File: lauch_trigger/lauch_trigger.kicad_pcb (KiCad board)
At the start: 2 copper layers, 39 x 22 mm, 6 parts, among them J1 jack_A, J2 jack_B, J3 conn_A, J4 conn_B

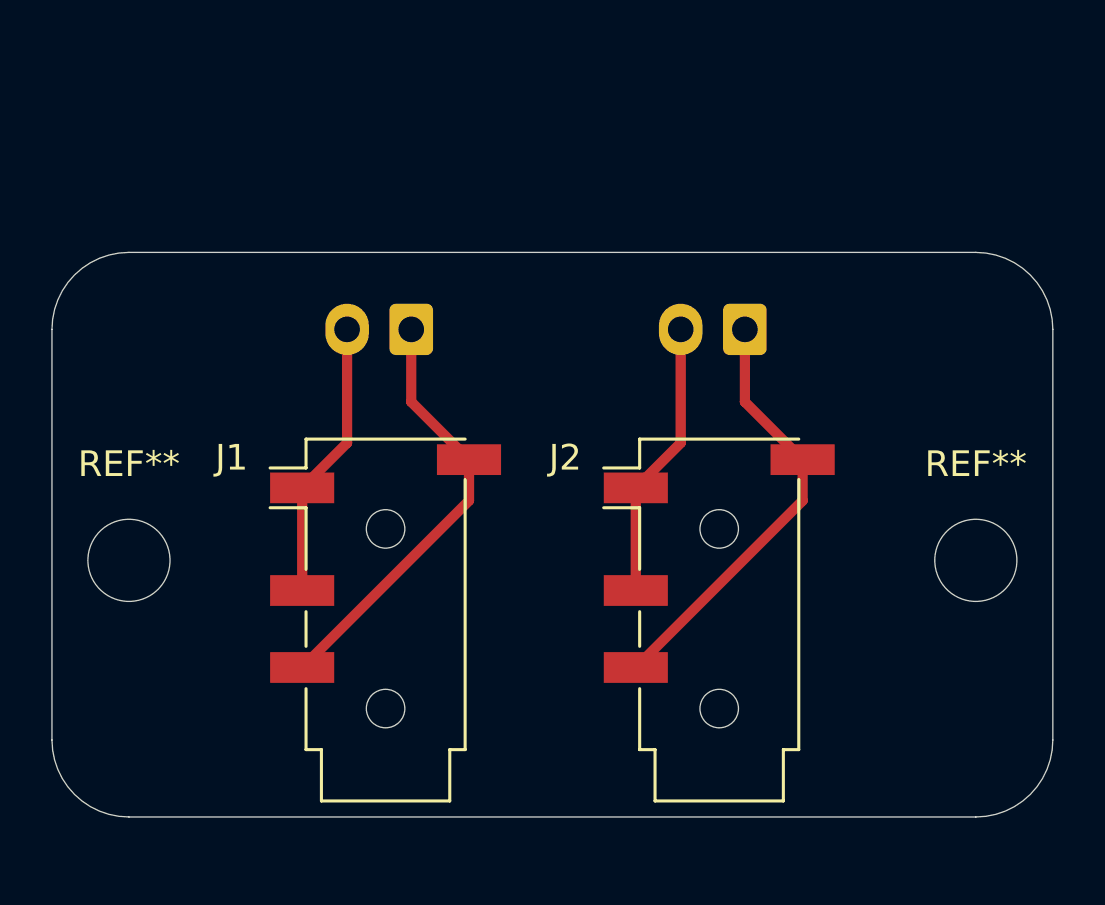
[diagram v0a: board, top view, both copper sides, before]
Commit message: Created PCB for jack connectors
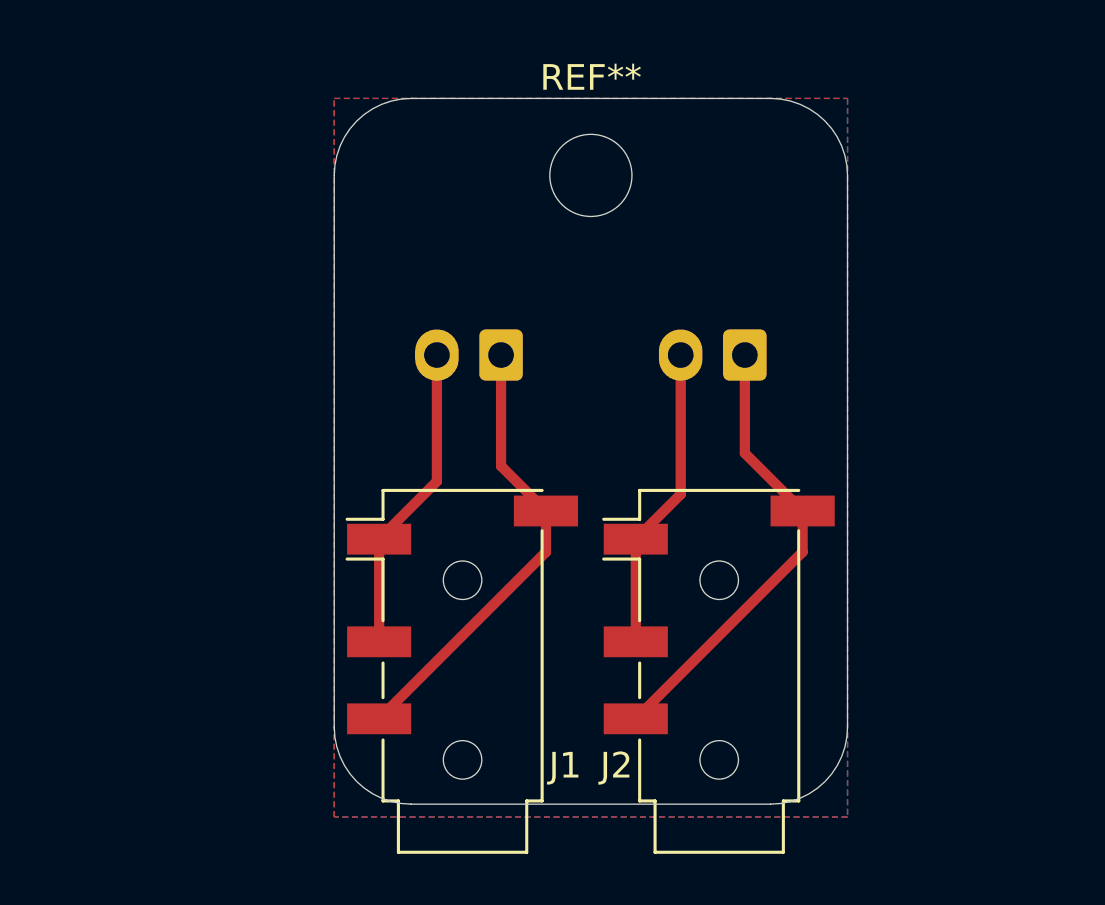
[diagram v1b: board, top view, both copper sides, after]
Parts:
- removed the REF** at (151.0, 93.0)
- removed the REF** at (118.0, 93.0)
- added REF**: MountingHole_3.2mm_M3_ISO7380, MountingHole:MountingHole_3.2mm_M3_ISO7380, F.Cu at (136.0, 78.0)
- J1, J2: footprint Connector_Audio:Jack_3.5mm_PJ320D_Horizontal -> nasa:Jack_3.5mm_PJ320D_Horizontal
- moved J3 3.64 mm to (132.5, 85.0)
- moved J1 3.61 mm to (131.0, 96.0)
- moved J2 2.00 mm to (141.0, 96.0)
- moved J4 1.00 mm to (142.0, 85.0)
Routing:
- net Net-(J3-Pin_2): track 10.9 -> 12.1 mm
- net Net-(J4-Pin_2): track 10.9 -> 11.9 mm
- net Net-(J4-Pin_1): track 16.8 -> 17.8 mm
- net Net-(J3-Pin_1): track 16.8 -> 17.6 mm
- added copper zone on B.Cu, net (none)
- added copper zone on F.Cu, net (none)
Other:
- board size 39 x 22 mm -> 20 x 27.5 mm
